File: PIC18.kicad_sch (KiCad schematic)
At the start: 75 parts, among them J1 Conn_02x20_Odd_Even, J10 Port B, J11 Port C, J12 Port D, J13 Conn_01x03, J14 Conn_01x03, J15 Conn_01x03, J16 Conn_01x03, J2 Conn_01x06, J3 USB_A, J4 Conn_01x03, J5 Conn_01x02, J6 Conn_01x02, J7 USB_OTG, J8 Port A, J9 Port E, U1 PIC18F4620, U2 LM4040DBZ-4.1, U3 FT230XS, Y1 8 MHz

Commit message: Routing
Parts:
- C6: value 100n -> 100nF
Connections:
- net GND: now also J13.1 (Pin_1)
- net RA1/AN1: no longer J4.2 (Pin_2)
- net RA3/AN3/VREF+: no longer J4.3 (Pin_3), J9.4 (Pin_4), R15.1, R16.1, R17.1, R18.1, R5.2, R6.2, U2.1 (K)
- net VCC: no longer J7.1 (VBUS)
- net at F1.1, J3.1 (VBUS): now also J7.1 (VBUS)
- new net: J4.3 (Pin_3), R5.2, R6.2, U2.1 (K)
- new net VREF+: J4.2 (Pin_2), J9.4 (Pin_4), R15.1, R16.1, R17.1, R18.1
- no-connect marks 6 -> 5
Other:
- moved on the sheet: F1

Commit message: Schematic edit
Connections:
- net RA3/AN3/VREF+: now also J4.2 (Pin_2)
- net VREF+: now also J4.3 (Pin_3), R5.2, R6.2, U2.1 (K); no longer J4.2 (Pin_2)
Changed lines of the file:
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@@
 	)
 	(no_connect
-		(at 257.81 66.04)
+		(at 247.65 66.04)
 	)
 	(wire
@@
 	(wire
 		(pts
+			(xy 247.65 68.58) (xy 265.43 68.58)
+		)
+		(stroke
+			(width 0)
+			(type default)
+		)
+	)
+	(wire
+		(pts
 			(xy 90.17 215.9) (xy 81.28 215.9)
 		)
@@
 	(wire
 		(pts
-			(xy 257.81 68.58) (xy 265.43 68.58)
-		)
-		(stroke
-			(width 0)
-			(type default)
-		)
-	)
-	(wire
-		(pts
 			(xy 198.12 160.02) (xy 217.17 160.02)
 		)
@@
 	(wire
 		(pts
-			(xy 257.81 66.04) (xy 265.43 66.04)
+			(xy 247.65 66.04) (xy 265.43 66.04)
 		)
 		(stroke
@@
 		)
 	)
+	(label "VREF+"
+		(at 267.97 78.74 180)
+		(fields_autoplaced yes)
+		(effects
+			(font
+				(size 1.27 1.27)
+			)
+			(justify right bottom)
+		)
+	)
 	(label "OSC1/CLKI/RA7"
 		(at 222.25 232.41 180)
@@
 		)
 	)
-	(label "VREF+"
-		(at 264.16 68.58 180)
-		(fields_autoplaced yes)
-		(effects
-			(font
-				(size 1.27 1.27)
-			)
-			(justify right bottom)
-		)
-	)
 	(label "RE2/CS*/AN7"
 		(at 142.24 162.56 180)
@@
 		)
 	)
+	(label "VREF+"
+		(at 264.16 71.12 180)
+		(fields_autoplaced yes)
+		(effects
+			(font
+				(size 1.27 1.27)
+			)
+			(justify right bottom)
+		)
+	)
 	(label "RD1/PSP1"
 		(at 237.49 240.03 0)
@@
 		(fields_autoplaced yes)
 		(effects
+			(font
+				(size 1.27 1.27)
+			)
+			(justify right bottom)
+		)
+	)
+	(label "RA3/AN3/VREF+"
+		(at 264.16 68.58 180)
+		(fields_autoplaced yes)
+		(effects

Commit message: All main wiring done
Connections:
- net GND: no longer J13.1 (Pin_1)
- net RC7/RX/DT: no longer J13.2 (Pin_2), U3.1 (TXD)
- new net ICTX: J13.2 (Pin_2), U3.1 (TXD)
- no-connect marks 5 -> 6
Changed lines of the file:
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@@
 	)
 	(no_connect
+		(at 309.88 66.04)
+	)
+	(no_connect
 		(at 92.71 104.14)
 	)
@@
 	(wire
 		(pts
-			(xy 306.07 66.04) (xy 323.85 66.04)
-		)
-		(stroke
-			(width 0)
-			(type default)
-		)
-	)
-	(wire
-		(pts
 			(xy 236.22 222.25) (xy 246.38 222.25)
 		)
@@
 	(wire
 		(pts
-			(xy 306.07 68.58) (xy 306.07 66.04)
-		)
-		(stroke
-			(width 0)
-			(type default)
-		)
-	)
-	(wire
-		(pts
 			(xy 318.77 91.44) (xy 323.85 91.44)
 		)
@@
 	(wire
 		(pts
+			(xy 309.88 66.04) (xy 323.85 66.04)
+		)
+		(stroke
+			(width 0)
+			(type default)
+		)
+	)
+	(wire
+		(pts
 			(xy 325.12 107.95) (xy 325.12 105.41)
 		)
@@
 		)
 	)
-	(label "RC7/RX/DT"
-		(at 321.31 68.58 180)
-		(fields_autoplaced yes)
-		(effects
-			(font
-				(size 1.27 1.27)
-			)
-			(justify right bottom)
-		)
-	)
 	(label "RB2/INT2/AN8"
 		(at 160.02 228.6 0)
@@
 		)
 	)
+	(label "ICTX"
+		(at 165.1 64.77 0)
+		(fields_autoplaced yes)
+		(effects
+			(font
+				(size 1.27 1.27)
+			)
+			(justify left bottom)
+		)
+	)
 	(label "RC3/SCK/SCL"
 		(at 90.17 259.08 180)
@@
 		)
 	)
+	(label "ICTX"
+		(at 321.31 68.58 180)
+		(fields_autoplaced yes)
+		(effects
+			(font
+				(size 1.27 1.27)
+			)
+			(justify right bottom)
+		)
+	)
 	(label "RB7/KBI3/PGD"
 		(at 44.45 78.74 0)
@@
 		)
 	)
-	(label "RC7/RX/DT"
-		(at 165.1 64.77 0)
-		(fields_autoplaced yes)
-		(effects
-			(font
-				(size 1.27 1.27)
-			)
-			(justify left bottom)
-		)
-	)
 	(label "RB0/INT0/FLT0/AN12"
 		(at 222.25 257.81 180)
@@
 					(unit 1)
 				)
-			)
-		)
-	)
-	(symbol
-		(lib_id "power:GND")
-		(at 306.07 68.58 0)
-		(unit 1)
-		(exclude_from_sim no)
-		(in_bom yes)
-		(on_board yes)
-		(dnp no)
-		(fields_autoplaced yes)
-		(property "Reference" "#PWR028"
-			(at 306.07 74.93 0)
-			(effects
-				(font
-					(size 1.27 1.27)
-				)
-				(hide yes)
-			)
-		)
-		(property "Value" "GND"
-			(at 306.07 73.66 0)
-			(effects
-				(font
-					(size 1.27 1.27)
-				)
-			)
-		)
-		(property "Footprint" ""
-			(at 306.07 68.58 0)
-			(effects
-				(font
-					(size 1.27 1.27)
-				)
-				(hide yes)
-			)
-		)
-		(property "Datasheet" ""
-			(at 306.07 68.58 0)
-			(effects
-				(font
-					(size 1.27 1.27)
-				)
-				(hide yes)
-			)
-		)
-		(property "Description" "Power symbol creates a global label with name \"GND\" , ground"
-			(at 306.07 68.58 0)
-			(effects
-				(font
-					(size 1.27 1.27)
-				)
-				(hide yes)
-			)
-		)
-		(pin "1"
-		)
-		(instances
-			(project "PIC18"
-				(path "/e4a6b067-3b9b-4409-bea0-0b6131f207b6"
-					(reference "#PWR028")
-					(unit 1)
-				)

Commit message: Silkscreen edits
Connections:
- net RC6/TX/CK: no longer J13.3 (Pin_3)
- net RC7/RX/DT: now also J13.3 (Pin_3)
- net ICTX renamed TXD
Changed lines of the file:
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@@
-		)
-	)
-	(label "RC6{slash}TX{slash}CK"
-		(at 321.31 71.12 180)
-		(fields_autoplaced yes)
-		(effects
-			(font
-				(size 1.27 1.27)
-			)
-			(justify right bottom)
 		)
 	)
@@
 		)
 	)
+	(label "RC7/RX/DT"
+		(at 321.31 71.12 180)
+		(fields_autoplaced yes)
+		(effects
+			(font
+				(size 1.27 1.27)
+			)
+			(justify right bottom)
+		)
+	)
 	(label "RE2/CS*/AN7"
 		(at 142.24 162.56 180)
@@
 		)
 	)
-	(label "ICTX"
+	(label "TXD"
 		(at 165.1 64.77 0)
 		(fields_autoplaced yes)
@@
 		)
 	)
-	(label "ICTX"
+	(label "TXD"
 		(at 321.31 68.58 180)
 		(fields_autoplaced yes)

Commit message: JLCPCB parody edits
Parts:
- C10, C12: value .1uf -> 100nf
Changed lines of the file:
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@@
 			)
 		)
-		(property "Value" ".1uf"
+		(property "Value" "100nf"
 			(at 55.88 217.932 0)
 			(effects
@@
 			)
 		)
-		(property "Value" ".1uf"
+		(property "Value" "100nf"
 			(at 50.546 217.932 0)
 			(effects

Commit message: more jlcpcb parody
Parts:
- D2: footprint LED_SMD:LED_0402_1005Metric -> LED_SMD:LED_0805_2012Metric
- R2, R3: value 27 -> 33
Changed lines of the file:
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@@
 		(dnp no)
 		(property "Reference" "R3"
-			(at 104.14 79.756 90)
+			(at 102.616 77.47 90)
 			(effects
 				(font
@@
 			)
 		)
-		(property "Value" "27"
-			(at 104.14 77.47 90)
+		(property "Value" "33"
+			(at 105.664 77.47 90)
 			(effects
 				(font
@@
 			)
 		)
-		(property "Footprint" "LED_SMD:LED_0402_1005Metric"
+		(property "Footprint" "LED_SMD:LED_0805_2012Metric"
 			(at 207.01 85.09 0)
 			(effects
@@
 			)
 		)
-		(property "Value" "27"
+		(property "Value" "33"
 			(at 105.664 70.358 90)
 			(effects

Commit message: Changed main pin header to pin socket
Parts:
- J1: footprint Connector_PinHeader_2.54mm:PinHeader_2x20_P2.54mm_Vertical -> PinSockets:PinSocket_2x20_Counter_Clockwise_P2.54mm_Vertical
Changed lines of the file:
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@@
 			)
 		)
-		(property "Footprint" "Connector_PinHeader_2.54mm:PinHeader_2x20_P2.54mm_Vertical"
+		(property "Footprint" "PinSockets:PinSocket_2x20_Counter_Clockwise_P2.54mm_Vertical"
 			(at 228.6 240.03 0)
 			(effects

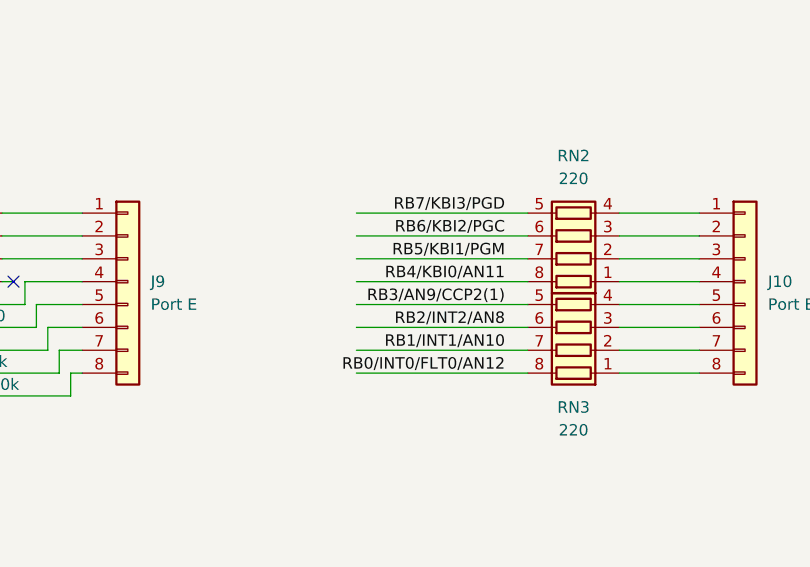
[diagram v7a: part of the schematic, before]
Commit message: fixed port B
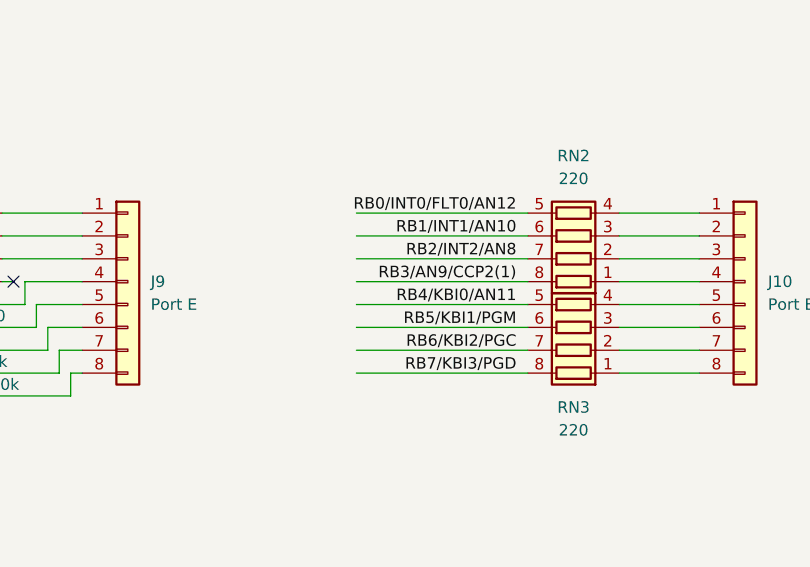
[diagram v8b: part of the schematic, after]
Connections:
- net RB0/INT0/FLT0/AN12: now also RN2.5 (R4.2); no longer RN3.8 (R1.2)
- net RB1/INT1/AN10: now also RN2.6 (R3.2); no longer RN3.7 (R2.2)
- net RB2/INT2/AN8: now also RN2.7 (R2.2); no longer RN3.6 (R3.2)
- net RB3/AN9/CCP2(1): now also RN2.8 (R1.2); no longer RN3.5 (R4.2)
- net RB4/KBI0/AN11: now also RN3.5 (R4.2); no longer RN2.8 (R1.2)
- net RB5/KBI1/PGM: now also RN3.6 (R3.2); no longer RN2.7 (R2.2)
- net RB6/KBI2/PGC: now also RN3.7 (R2.2); no longer RN2.6 (R3.2)
- net RB7/KBI3/PGD: now also RN3.8 (R1.2); no longer RN2.5 (R4.2)
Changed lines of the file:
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@@
+		)
+	)
+	(label "RB2{slash}INT2{slash}AN8"
+		(at 215.9 162.56 180)
+		(fields_autoplaced yes)
+		(effects
+			(font
+				(size 1.27 1.27)
+			)
+			(justify right bottom)
 		)
 	)
@@
 		)
 	)
-	(label "RB5{slash}KBI1{slash}PGM"
-		(at 214.63 162.56 180)
-		(fields_autoplaced yes)
-		(effects
-			(font
-				(size 1.27 1.27)
-			)
-			(justify right bottom)
-		)
-	)
-	(label "RB2{slash}INT2{slash}AN8"
-		(at 214.63 170.18 180)
-		(fields_autoplaced yes)
-		(effects
-			(font
-				(size 1.27 1.27)
-			)
-			(justify right bottom)
-		)
-	)
-	(label "RB1{slash}INT1{slash}AN10"
-		(at 214.63 172.72 180)
-		(fields_autoplaced yes)
-		(effects
-			(font
-				(size 1.27 1.27)
-			)
-			(justify right bottom)
-		)
-	)
 	(label "RD5/PSP5/P1B"
 		(at 339.09 170.18 180)
@@
 		)
 	)
+	(label "RB6{slash}KBI2{slash}PGC"
+		(at 215.9 172.72 180)
+		(fields_autoplaced yes)
+		(effects
+			(font
+				(size 1.27 1.27)
+			)
+			(justify right bottom)
+		)
+	)
 	(label "RC4{slash}SDI{slash}SDA"
 		(at 307.34 93.98 180)
@@
 		)
 	)
-	(label "RB0{slash}INT0{slash}FLT0{slash}AN12"
-		(at 214.63 175.26 180)
-		(fields_autoplaced yes)
-		(effects
-			(font
-				(size 1.27 1.27)
-			)
-			(justify right bottom)
-		)
-	)
 	(label "RD4/PSP4"
 		(at 160.02 248.92 0)
@@
 		)
 	)
+	(label "RB1{slash}INT1{slash}AN10"
+		(at 215.9 160.02 180)
+		(fields_autoplaced yes)
+		(effects
+			(font
+				(size 1.27 1.27)
+			)
+			(justify right bottom)
+		)
+	)
 	(label "RC4{slash}SDI{slash}SDA"
 		(at 276.86 167.64 180)
@@
 		)
 	)
-	(label "RB4{slash}KBI0{slash}AN11"
-		(at 214.63 165.1 180)
-		(fields_autoplaced yes)
-		(effects
-			(font
-				(size 1.27 1.27)
-			)
-			(justify right bottom)
-		)
-	)
 	(label "RD3/PSP3"
 		(at 237.49 242.57 0)
@@
 		)
 	)
+	(label "RB0{slash}INT0{slash}FLT0{slash}AN12"
+		(at 215.9 157.48 180)
+		(fields_autoplaced yes)
+		(effects
+			(font
+				(size 1.27 1.27)
+			)
+			(justify right bottom)
+		)
+	)
 	(label "RC2/CCP1/P1A"
 		(at 90.17 256.54 180)
@@
 		)
 	)
-	(label "RB7{slash}KBI3{slash}PGD"
-		(at 214.63 157.48 180)
-		(fields_autoplaced yes)
-		(effects
-			(font
-				(size 1.27 1.27)
-			)
-			(justify right bottom)
-		)
-	)
 	(label "RE0/RD*/AN5"
 		(at 90.17 233.68 180)
@@
 		)
 	)
+	(label "RB4{slash}KBI0{slash}AN11"
+		(at 215.9 167.64 180)
+		(fields_autoplaced yes)
+		(effects
+			(font
+				(size 1.27 1.27)
+			)
+			(justify right bottom)
+		)
+	)
 	(label "OSC1/CLKI/RA7"
 		(at 222.25 232.41 180)
@@
 		)
 	)
+	(label "RB3{slash}AN9{slash}CCP2(1)"
+		(at 215.9 165.1 180)
+		(fields_autoplaced yes)
+		(effects
+			(font
+				(size 1.27 1.27)
+			)
+			(justify right bottom)
+		)
+	)
+	(label "RB7{slash}KBI3{slash}PGD"
+		(at 215.9 175.26 180)
+		(fields_autoplaced yes)
+		(effects
+			(font
+				(size 1.27 1.27)
+			)
+			(justify right bottom)
+		)
+	)
 	(label "TXD"
 		(at 321.31 68.58 180)
@@
 		)
 	)
+	(label "RB5{slash}KBI1{slash}PGM"
+		(at 215.9 170.18 180)
+		(fields_autoplaced yes)
+		(effects
+			(font
+				(size 1.27 1.27)
+			)
+			(justify right bottom)
+		)
+	)
 	(label "RB6/KBI2/PGC"
 		(at 44.45 81.28 0)
@@
 		)
 	)
-	(label "RB6{slash}KBI2{slash}PGC"
-		(at 214.63 160.02 180)
-		(fields_autoplaced yes)
-		(effects
-			(font
-				(size 1.27 1.27)
-			)
-			(justify right bottom)
-		)
-	)
 	(label "VTHERM"
 		(at 254 88.9 0)
@@
 		)
 	)
-	(label "RB3{slash}AN9{slash}CCP2(1)"
-		(at 214.63 167.64 180)
-		(fields_autoplaced yes)
-		(effects
-			(font
-				(size 1.27 1.27)
-			)
-			(justify right bottom)
-		)
-	)
